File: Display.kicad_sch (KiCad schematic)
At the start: 1 part, among them J3 Conn_01x04_Pin

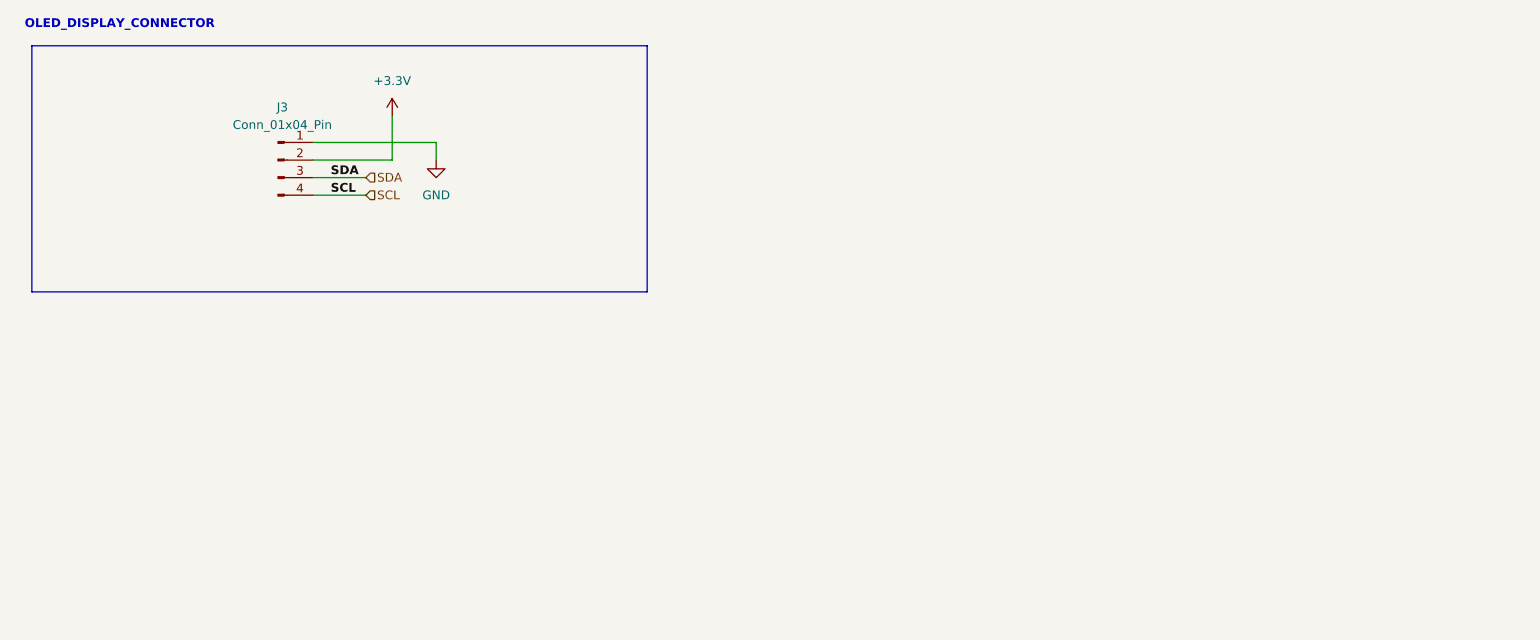
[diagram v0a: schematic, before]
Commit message: refactor(sch): replace +3.3V power symbol with 7-pin connector
Replaces the global +3.3V power symbol with a physical 1x07 connector symbol in the Display schematic.
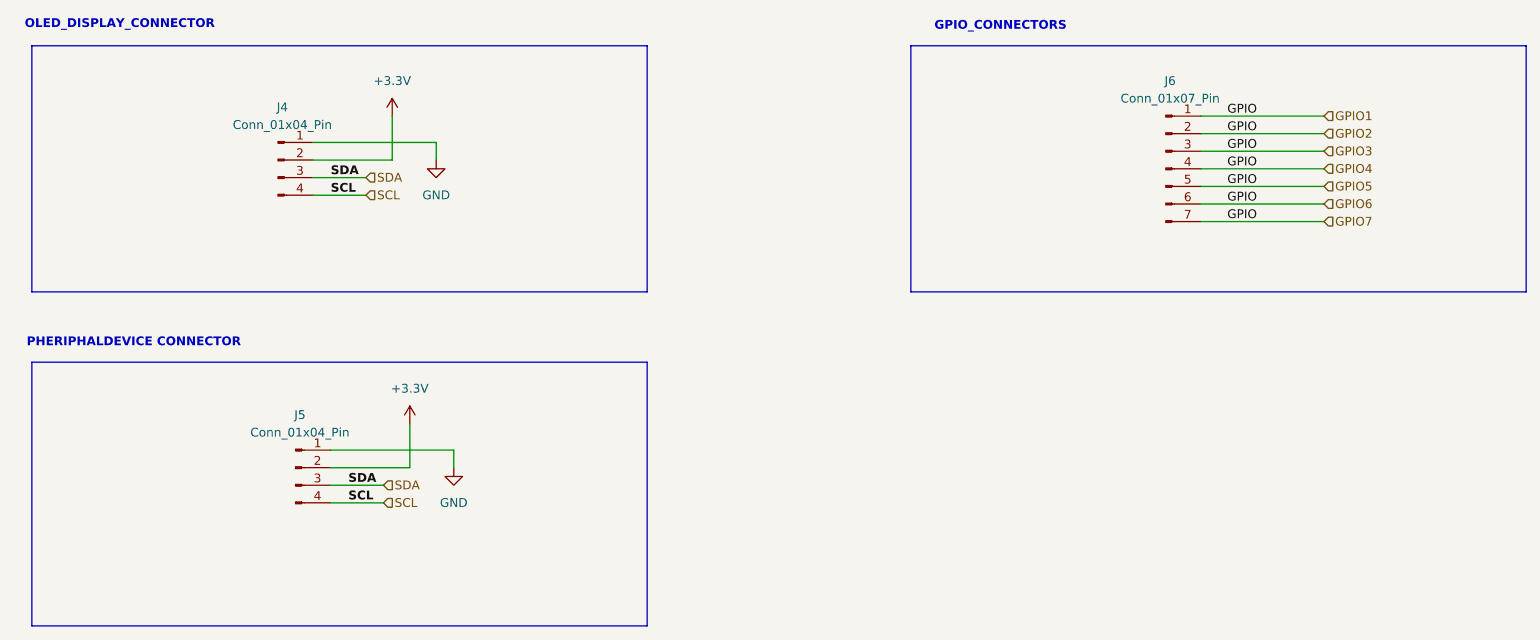
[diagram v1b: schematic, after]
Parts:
- added J5: Conn_01x04_Pin, Connector_JST:JST_SH_SM04B-SRSS-TB_1x04-1MP_P1.00mm_Horizontal, symbol Connector:Conn_01x04_Pin
- added J6: Conn_01x07_Pin, TerminalBlock_Phoenix:TerminalBlock_Phoenix_MKDS-1,5-7-5.08_1x07_P5.08mm_Horizontal, symbol Connector:Conn_01x07_Pin
- renumbered J3 to J4
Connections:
- net +3.3V: now also J5.2 (Pin_2)
- net GND: now also J5.1 (Pin_1)
- net SCL: now also J5.4 (Pin_4)
- net SDA: now also J5.3 (Pin_3)
- new net GPIO1: J6.1 (Pin_1), J6.2 (Pin_2), J6.3 (Pin_3), J6.4 (Pin_4), J6.5 (Pin_5), J6.6 (Pin_6), J6.7 (Pin_7)
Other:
- note added: "GPIO_CONNECTORS"
- note added: "PHERIPHALDEVICE CONNECTOR"
